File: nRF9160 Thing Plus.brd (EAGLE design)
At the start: 58.4 x 22.9 mm, 129 parts, among them J1 USB Female C, J10 QWIIC_RIGHT_ANGLE, J2 CON-HEADER-1X12-MALE-PIN, J3 CON-HEADER-1X16-MALE-PIN, J4 CON-1909763-1, J7 CON-1909763-1, J9 CON-0002, P1 CON-SIM-SF72S006VBAR2500, Q1 MOSFET-P-SC89, Q2 MOSFET-DUAL-COMP-SOT563, Q3 MOSFET-P-20V-4.7A-SOT23, Q4 MOSFET-N-SC89, Q5 MOSFET-N-SC89, SW1 MOMENTARY-SWITCH-SPST-SMD-4.6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, SW2 MOMENTARY-SWITCH-SPST-SMD-4.6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, U1 MOD-NRF9160-SICA-R, U10 IC-SIM-ST-MFF2, U11 IC-EMIF03-SIM02M8, U12 IC-LIS2DH12TR, U2 MCP73831, U3 IC-TPS63031DSKR, U4 POWER-SWITCH-MIC94092YC6, U5 IC-CP2102N-A02-GQFN24R, U6 FLASH-W25Q16JVZPIQ-WSON, U7 IC-NX3DV2567GU, U8 IC-PCF85063ATL/1, U9 IC-BAV70S, Y1 XTAL-ABS07AIG-32.768KHZ-7-T

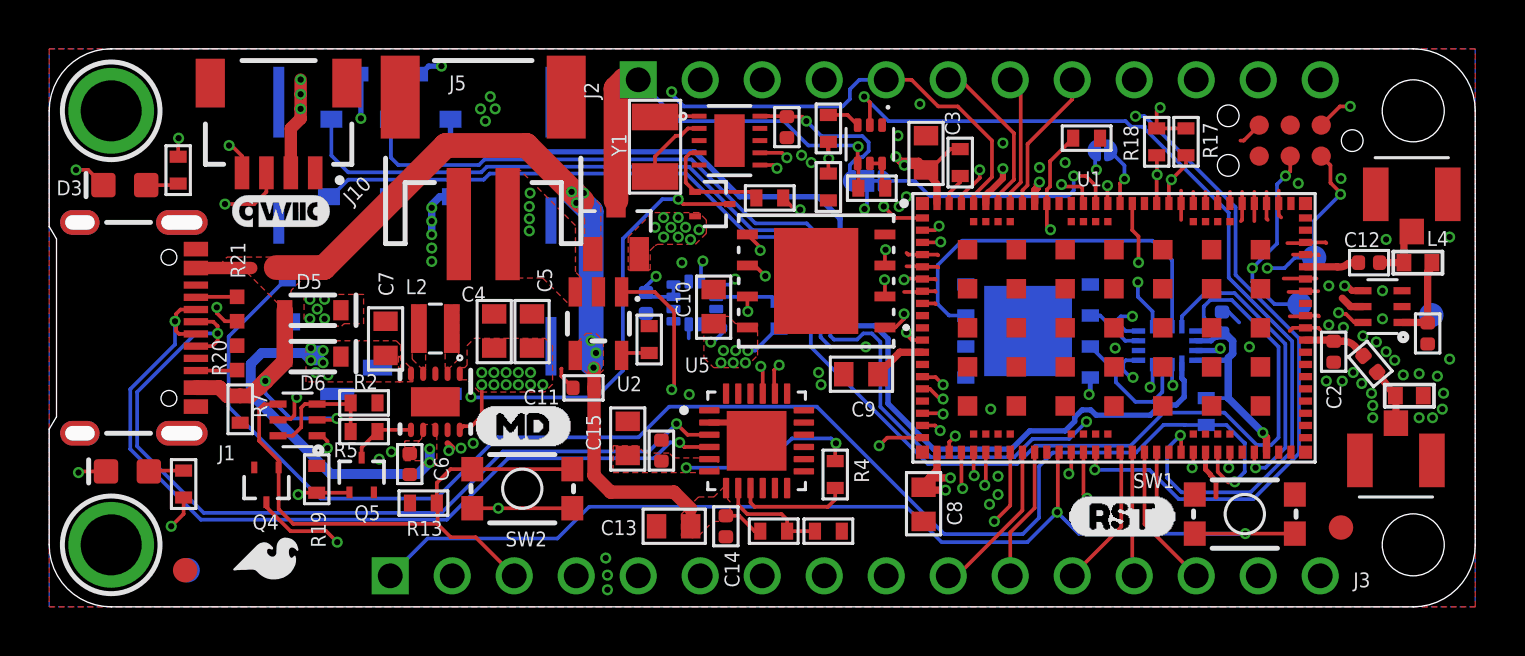
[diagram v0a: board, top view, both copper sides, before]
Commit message: Thing Plus label
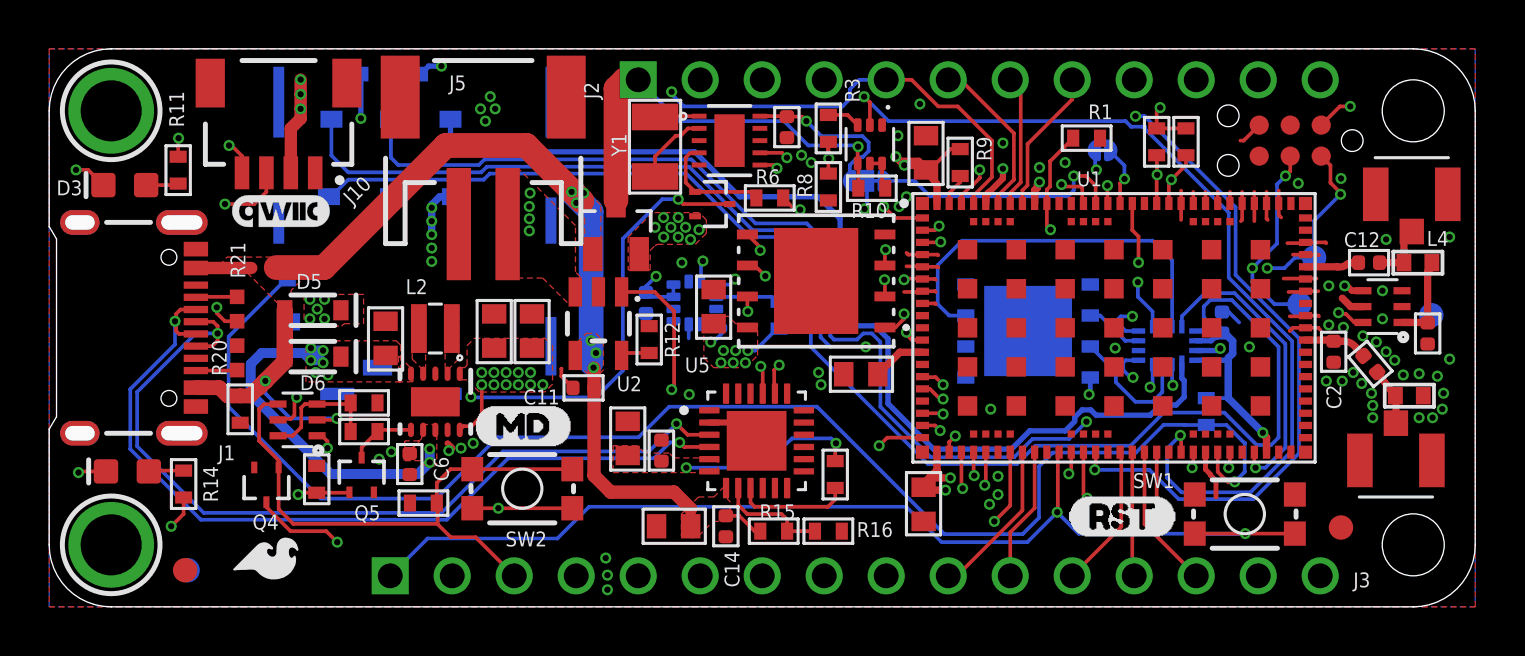
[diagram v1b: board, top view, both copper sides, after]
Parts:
- added U$25: (no value), buzzard_labels-21:NRF9160_THING_PLUS0

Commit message: Updated name label and eSIM cream
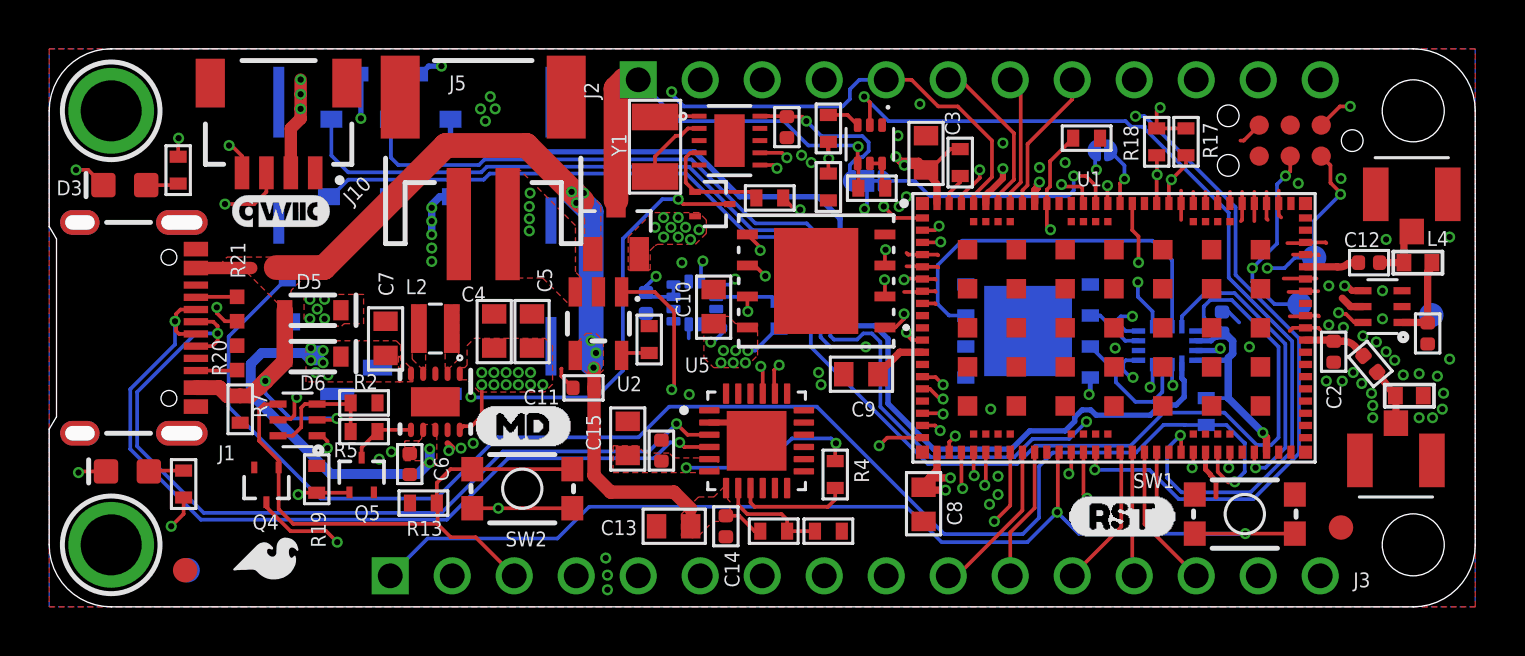
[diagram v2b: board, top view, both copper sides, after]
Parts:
- removed U$25: (no value), buzzard_labels-21:NRF9160_THING_PLUS0
- added U$23: (no value), output:NRF9160_THING_PLUS0
- U10: device wolff-den:PSON127P500X600X82-9N -> nrF9160 Thing Plus temp:PSON127P500X600X82-9N_NO_CREAM

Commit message: Moved components to local libraries
Parts not in SFE Eagle libraries were moved to local temporary libraries with the SFE SKUs added for the BOM
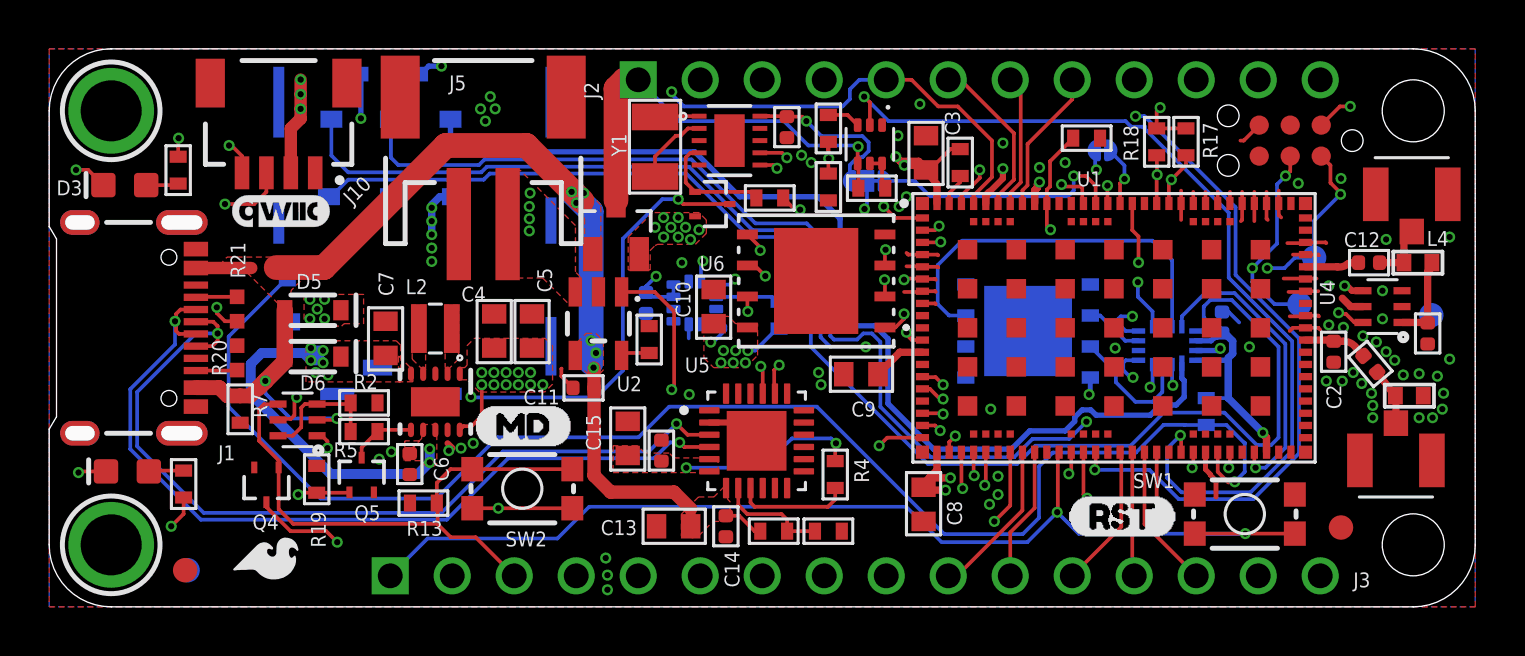
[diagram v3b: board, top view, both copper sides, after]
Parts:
- C1, C11, C12, C14, C16, C17, C18, C19, C2, C20, C6: device wolff-den:CAPC1005X55N -> nRF9160-Capacitors:CAPC1005X55N
- C10, C13, C15, C3, C4, C5, C7, C8, C9: device wolff-den:C0603 -> nRF9160-Capacitors:C0603
- J4, J7: device wolff-den:TE_1909763-1 -> nRF9160-Connectors:TE_1909763-1
- L1, L4: device wolff-den:IND0402_22N_TAI -> nRF9160-Coils:IND0402_22N_TAI
- L2: device wolff-den:IND-2P0X2P0X1P2 -> nRF9160-Coils:IND-2P0X2P0X1P2
- P1: device wolff-den:JAE_SF72S006VBAR2500 -> nRF9160-Connectors:JAE_SF72S006VBAR2500
- Q1, Q4, Q5: device wolff-den:DIO_RB558WMF-L -> nRF9160-DiscreteSemi:DIO_RB558WMF-L
- Q2: device wolff-den:SOT50P160X60-6N -> nRF9160-DiscreteSemi:SOT50P160X60-6N
- Q3: device wolff-den:SOT23 -> nRF9160-DiscreteSemi:SOT23
- R1, R10, R11, R12, R13, R14, R15, R16, R17, R18, R19, R2, R22, R23, R3, R4, R5, R6, R7, R8, R9: device wolff-den:R0402-M -> nRF9160-Resistors:R0402-M
- U1: device wolff-den:NORDIC_NRF9160-SICA-R -> nRF9160-IC:NORDIC_NRF9160-SICA-R
- U11: device wolff-den:SON40P170X150X60-9N -> nRF9160-IC:SON40P170X150X60-9N
- U12: device wolff-den:PQFN50P200X200100-12N -> nRF9160-IC:PQFN50P200X200100-12N
- U3: device wolff-den:DSK0010A -> nRF9160-IC:DSK0010A
- U4: device wolff-den:SOT363 -> nRF9160-IC:SOT363
- U5: device wolff-den:QFN50P400X400X80-25N -> nRF9160-IC:QFN50P400X400X80-25N
- U6: value FLASH-W25Q16JVZPIQ-WSON -> FLASH-W25Q128JVPIM-WSON; device wolff-den:WIN_ZP-8-L -> nRF9160-IC:WIN_ZP-8-L
- U7: device wolff-den:QFN40P260X180X50-16N -> nRF9160-IC:QFN40P260X180X50-16N
- U8: device wolff-den:DFN10_2P7X2P7-L -> nRF9160-IC:DFN10_2P7X2P7-L
- U9: device wolff-den:SOT363 -> nRF9160-DiscreteSemi:SOT363
- Y1: device wolff-den:XTAL320X150X90 -> nRF9160-Clocks:XTAL320X150X90

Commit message: Updating SDA/SCL labels
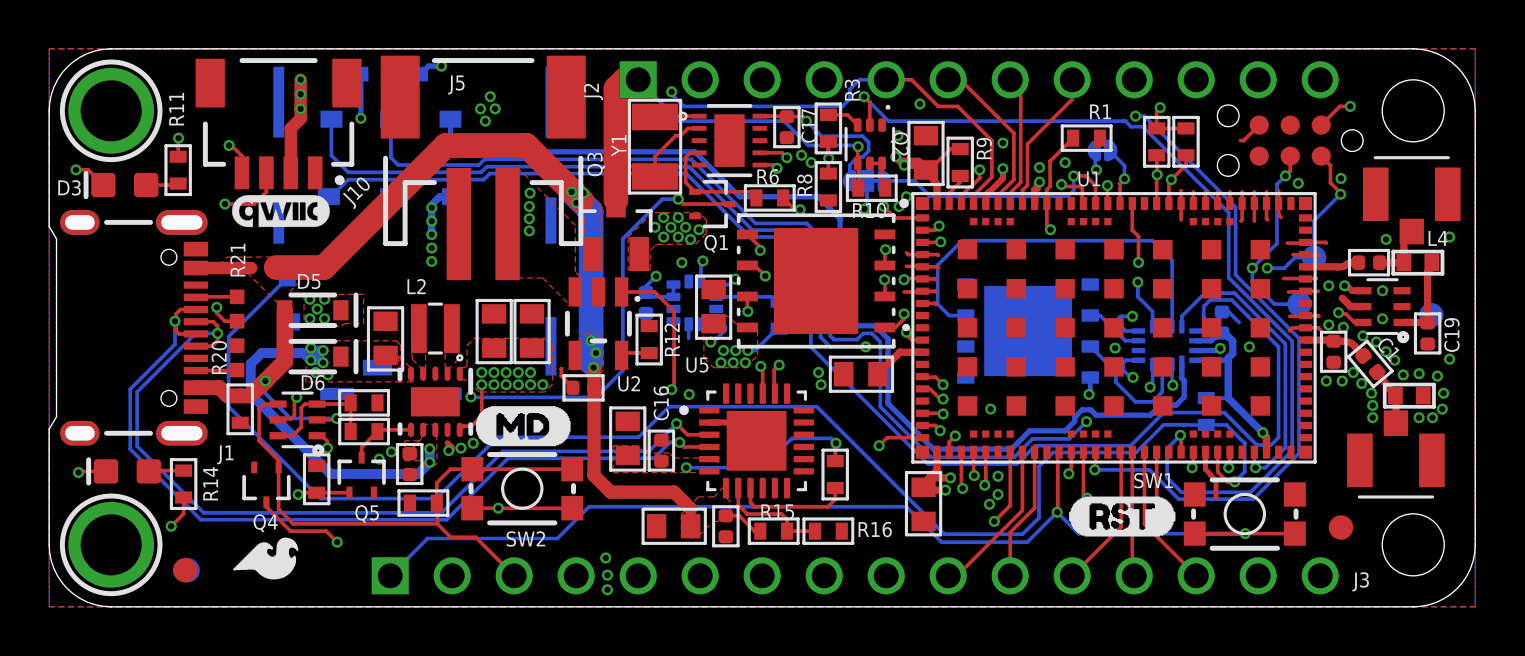
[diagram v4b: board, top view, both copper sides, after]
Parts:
- removed U$12: (no value), buzzard_labels-3:1#SDA0
- removed U$13: (no value), buzzard_labels-4:2#SCL0
- added U$24: (no value), buzzard_labels-2:1#SCL0
- added U$25: (no value), buzzard_labels:0#SDA0

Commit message: Adding Cortex-m header. Removing tag connect. Removing external SIM bits. Changing SIM holder to cheaper variant.
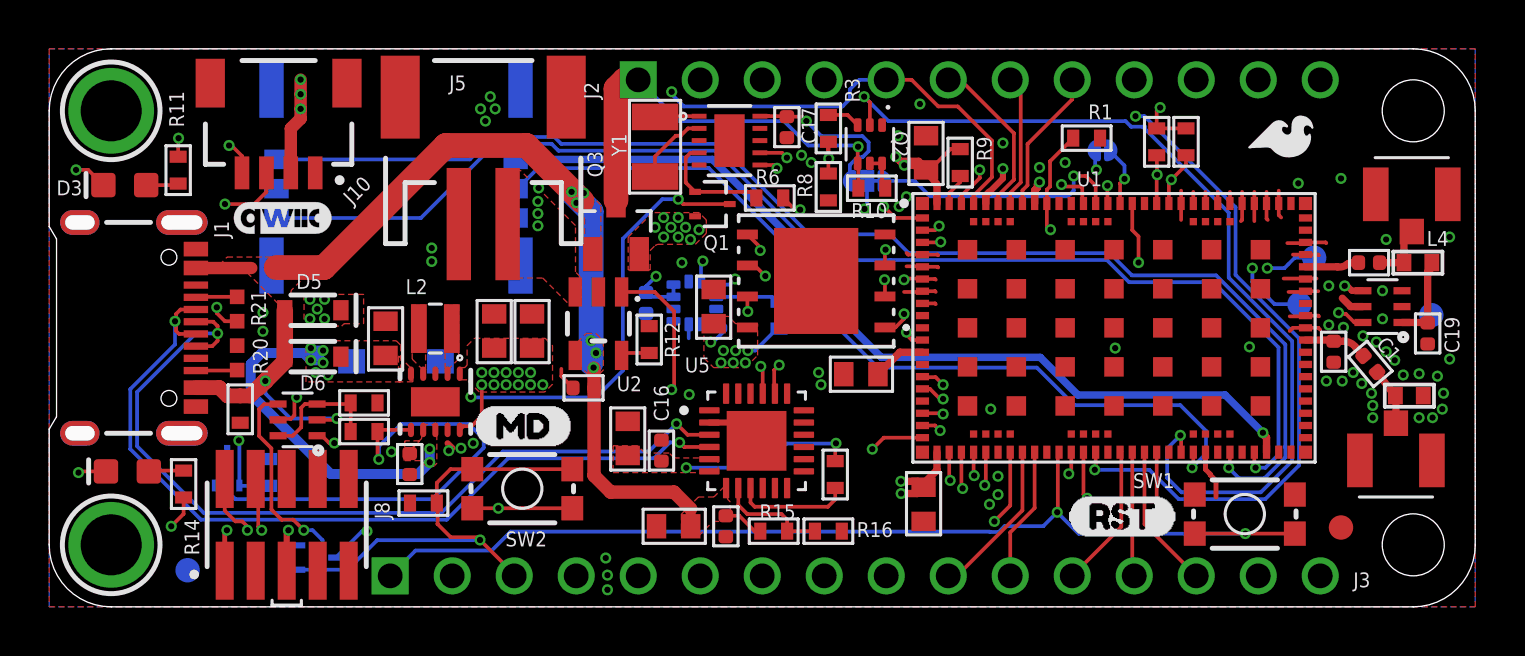
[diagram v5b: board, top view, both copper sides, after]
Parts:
- removed C18: 0.1u, nRF9160-Capacitors:CAPC1005X55N
- removed J9: CON-0002, wolff-den:TC2030-MCP-NL
- removed P1: CON-SIM-SF72S006VBAR2500, nRF9160-Connectors:JAE_SF72S006VBAR2500
- removed R22: 1M, nRF9160-Resistors:R0402-M
- removed SOLDER1: SOLDER-PASTE-ROOM-TEMP-50G, wolff-den:PLACEHOLDER
- removed U$34: FIDUCIAL-1MM, wolff-den:FIDUCIAL-1MM
- removed U10: IC-SIM-ST-MFF2, nrF9160 Thing Plus temp:PSON127P500X600X82-9N_NO_CREAM
- removed U11: IC-EMIF03-SIM02M8, nRF9160-IC:SON40P170X150X60-9N
- removed U7: IC-NX3DV2567GU, nRF9160-IC:QFN40P260X180X50-16N
- added J6: CON-SIM-104224-0820, wolff-den:MOLEX_104224-0820
- added J8: CON-FTSH-105-XX-X-DV, wolff-den:SAMTEC_FTSH-105-XX-X-DV
- moved U$15 45.0 mm to (50.6, 19.1)
- moved U$23 21.9 mm to (29.0, 7.64), turned to 0 degrees
- moved U$1 18.3 mm to (44.3, 8.44)
- moved LOGO5 18.3 mm to (6.50, 20.5)
- moved Q5 5.52 mm to (7.29, 5.68), flipped to the bottom
- moved Q4 3.62 mm to (11.0, 2.02), flipped to the bottom, turned to 90 degrees
- moved R19 1.99 mm to (8.99, 5.50), flipped to the bottom
- moved U$2 1.20 mm to (46.9, 13.2)
- moved U$6 0.29 mm to (9.57, 15.9)
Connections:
- removed net SIM_EMB_CLK: U10.6, U7.7
- removed net SIM_EMB_IO: U10.3, U7.11
- removed net SIM_EMB_RST: U10.7, U7.3
- removed net SIM_EMB_VCC: U10.8, U7.15
- removed net SIM_HLDR_CLK: U11.3, U7.9
- removed net SIM_HLDR_CLK_F: P1.C3, U11.6
- removed net SIM_HLDR_IO: U11.4, U7.13
- removed net SIM_HLDR_IO_F: P1.C7, U11.5
- removed net SIM_HLDR_RST: U11.2, U7.5
- removed net SIM_HLDR_RST_F: P1.C2, U11.7
- removed net SIM_HLDR_VCC: P1.C1, U11.1, U11.8, U7.1
- net +3V3: now also J8.1; no longer J9.1
- net GND: now also J6.G1, J6.G2, J6.G3, J6.G4, J6.S4, J8.3, J8.5, J8.9; no longer C18.2, J9.5, P1.C5, P1.DSW, P1.G1, P1.G10, P1.G2, P1.G3, P1.G4, P1.G5, P1.G6, P1.G7, P1.G8, P1.G9, U10.1, U10.9, U11.9, U7.6
- net SIM_CLK: now also J6.S3; no longer U7.8
- net SIM_DET: no longer P1.CSW, R22.2, U7.2
- net SIM_IO: now also J6.S6; no longer U7.12
- net SIM_RST: now also J6.S2; no longer U7.4
- net SIM_VCC: now also J6.S1; no longer C18.1, R22.1, U7.14, U7.16
- net SWCLK: now also J8.4; no longer J9.4
- net SWDIO: now also J8.2; no longer J9.2
- net VPP: now also J6.S5; no longer P1.C6
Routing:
- net SIM_DET: track 73.2 -> 0.00 mm, vias 2 -> 0
- net SIM_HLDR_VCC: track 42.5 -> 0.00 mm
- net SIM_IO: track 12.4 -> 52.0 mm
- net SIM_CLK: track 14.3 -> 53.4 mm, vias 2 -> 1
- net SWCLK: track 24.6 -> 62.0 mm
- net SWDIO: track 26.0 -> 61.1 mm
- net SIM_HLDR_IO: track 33.9 -> 0.00 mm
- net SIM_VCC: track 9.64 -> 36.8 mm
- net SIM_RST: track 11.0 -> 36.2 mm, vias 2 -> 1
- net SIM_HLDR_CLK_F: track 23.8 -> 0.00 mm
- net SIM_HLDR_RST: track 22.4 -> 0.00 mm, vias 2 -> 0
- net SIM_HLDR_IO_F: track 22.0 -> 0.00 mm
- net SIM_HLDR_RST_F: track 21.8 -> 0.00 mm
- net PS_EN: track 2.74 -> 21.5 mm, vias 0 -> 1
- net SIM_HLDR_CLK: track 18.5 -> 0.00 mm, vias 2 -> 0
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
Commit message: Moving programming header up to get away from board edge.
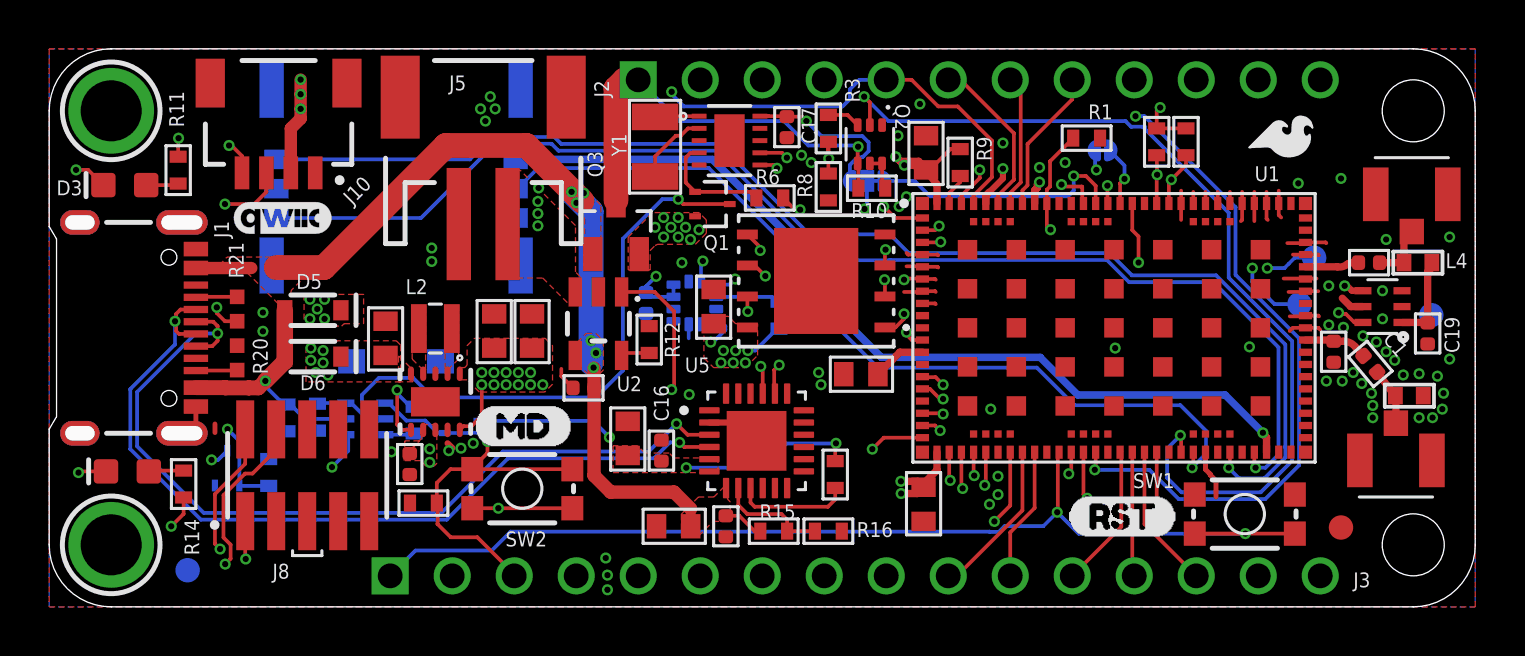
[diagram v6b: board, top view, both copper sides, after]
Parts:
- moved Q4 8.17 mm to (16.9, 7.62)
- moved U9 2.78 mm to (12.9, 7.70), flipped to the bottom
- moved J8 2.20 mm to (10.6, 5.39)
- moved R5 2.10 mm to (14.9, 7.65), flipped to the bottom, turned to 270 degrees
- moved R2 2.00 mm to (11.0, 7.77), flipped to the bottom, turned to 90 degrees
- moved R7 1.95 mm to (9.75, 7.74), flipped to the bottom
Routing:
- net MODE/WAKE: track 28.8 -> 18.1 mm, vias 2 -> 1
- net VSYS: track 60.2 -> 50.1 mm
- net PS_EN: track 21.5 -> 12.7 mm, vias 1 -> 2
- net P0.12/MD: track 26.1 -> 19.2 mm
- net SWDIO: track 61.1 -> 64.8 mm
- net SWCLK: track 62.0 -> 65.7 mm
- net RTC_PS_EN: track 26.0 -> 23.8 mm, vias 3 -> 1
- net NRF_PS_EN_JMP: track 29.3 -> 30.8 mm
- net VBUS: track 48.6 -> 49.8 mm, vias 8 -> 7
- net !EN: track 30.8 -> 31.9 mm
- net CHRG: track 32.6 -> 33.2 mm
- net PS_EN_CC: track 5.41 -> 4.83 mm
- net GND: track 36.9 -> 37.2 mm, vias 68 -> 67
